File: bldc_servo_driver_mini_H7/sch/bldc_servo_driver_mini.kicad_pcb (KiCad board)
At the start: 4 copper layers, 35 x 40 mm, 68 parts, among them IC1 ST730MR, IC2 LDK320AM50R, IC3 TLT9251VLEXUMA1, J1 1-2328702-0, J2 Conn_01x04, J3 Conn_01x04, J4 Conn_01x06, J5 Conn_01x03, J6 Conn_01x02, J7 DF65-3P-1.7V_21_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

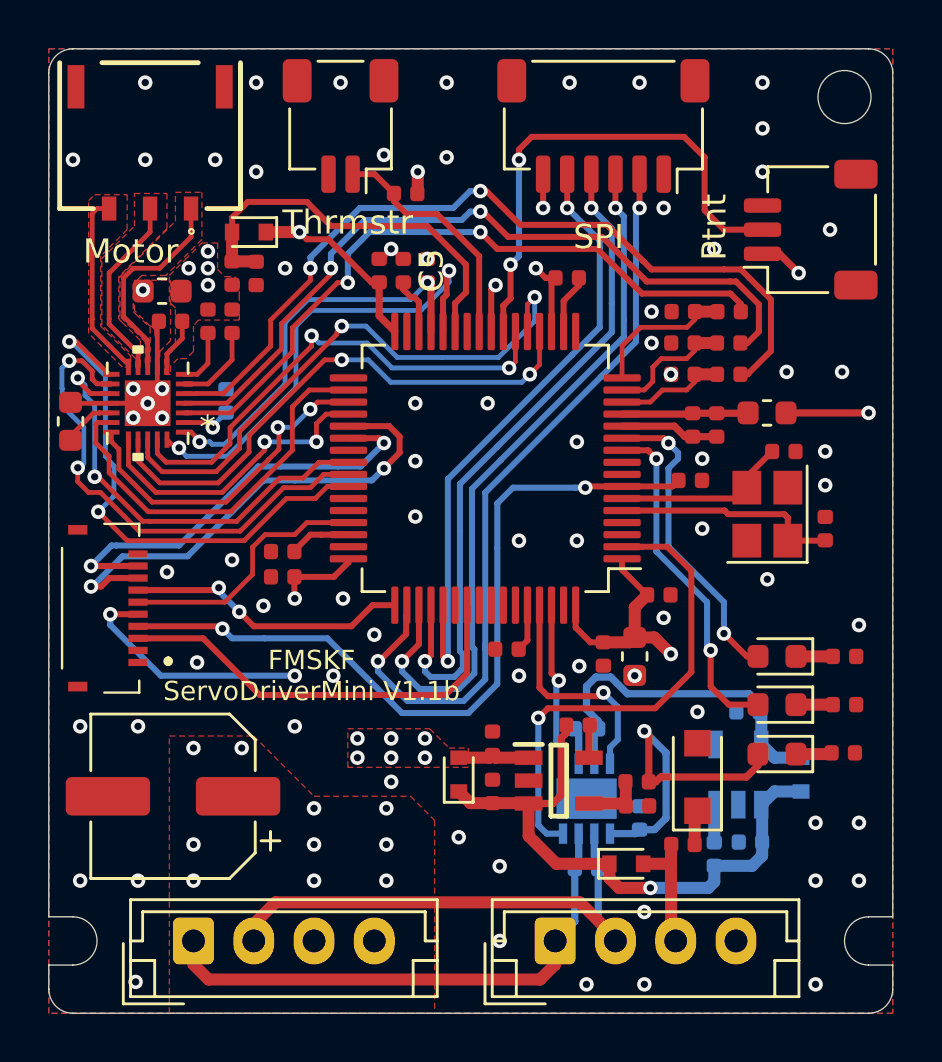
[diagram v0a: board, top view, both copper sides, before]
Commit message: fix : [H7sch] apply F4sch update to H7sch
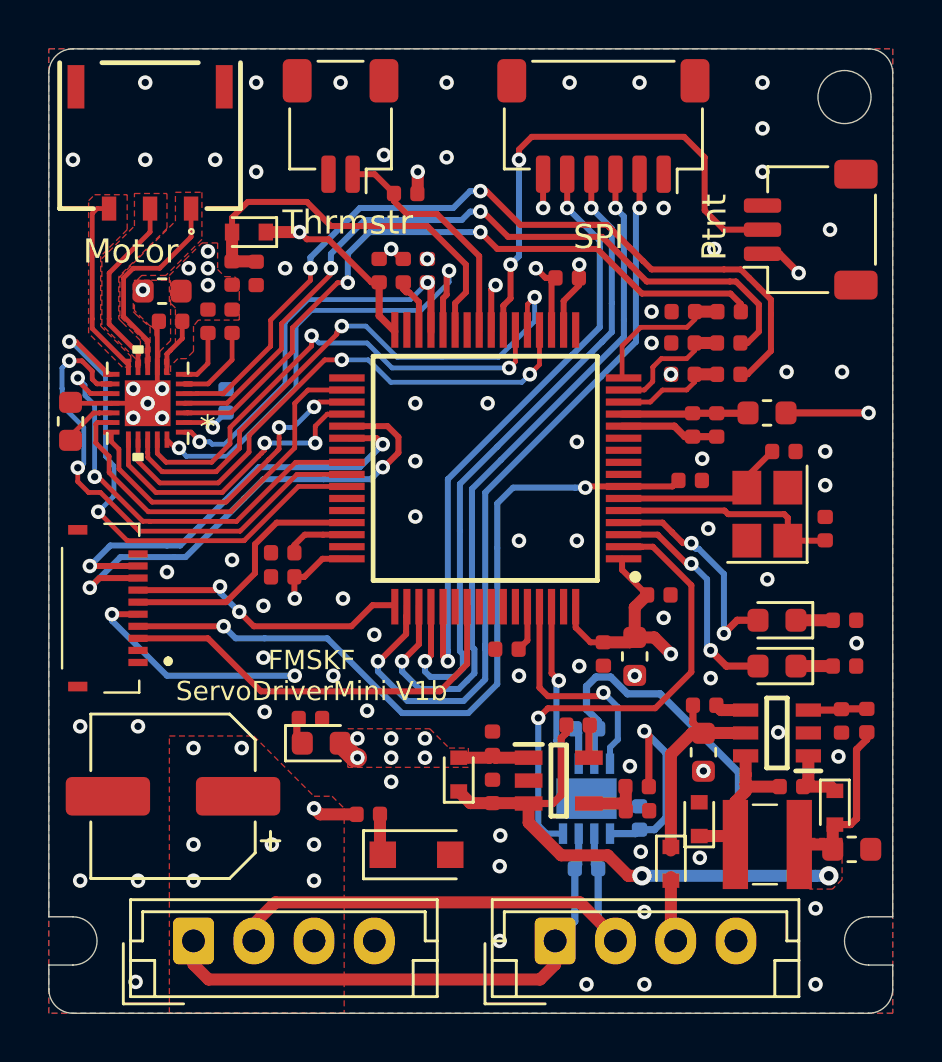
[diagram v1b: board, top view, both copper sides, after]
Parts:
- added C29: 10u, Capacitor_SMD:C_0603_1608Metric, F.Cu at (133.3, 93.2)
- added D9: D_Schottky, Diode_SMD:D_SOD-523, F.Cu at (132.6, 91.5)
- added L2: 4.7u, SamacSys_Parts:LPS3314332MRC, F.Cu at (129.8, 93.0)
- added R19: 30.1k, Resistor_SMD:R_0402_1005Metric, F.Cu at (133.9, 87.9)
- added R20: 10k, Resistor_SMD:R_0402_1005Metric, F.Cu at (132.9, 87.9)
- C15: value 1u -> 10u; footprint Capacitor_SMD:C_0402_1005Metric -> Capacitor_SMD:C_0603_1608Metric; moved to F.Cu
- C6: value 0.1u -> 0.01u; moved to F.Cu
- D2: value D_Schottky -> PMEG6010AESBYL
- D4, R3: moved to F.Cu
- IC2: value LDK320AM50R -> LT1616ES6#TRMPBF; footprint SamacSys_Parts:SOT95P280X145-5N -> SamacSys_Parts:SOT95P280X90-6N; moved to F.Cu
- U1: footprint Package_QFP:LQFP-64_10x10mm_P0.5mm -> SamacSys_Parts:QFP50P1200X1200X160-64N
- moved R14 22.1 mm to (110.8, 87.8)
- moved D8 18.9 mm to (111.3, 88.8), turned to 0 degrees
- moved R1 13.1 mm to (113.2, 91.8)
- moved C5 12.7 mm to (109.7, 80.9), turned to 180 degrees
- moved C2 12.7 mm to (114.7, 69.2), turned to 270 degrees
- moved D1 12.1 mm to (115.2, 93.4), turned to 0 degrees
- moved R3 6.19 mm to (127.2, 87.2), turned to 180 degrees
- moved D4 4.61 mm to (127.0, 92.0)
- moved C6 2.86 mm to (130.8, 90.6)
- moved C15 2.50 mm to (127.2, 89.2), turned to 90 degrees
- moved IC2 2.35 mm to (130.2, 88.4), turned to 180 degrees
- moved D2 1.85 mm to (125.8, 93.8), turned to 270 degrees
- moved D6 1.60 mm to (130.2, 85.6)
- moved R12 1.60 mm to (133.0, 85.6)
- moved D7 1.50 mm to (130.2, 83.7)
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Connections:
- C15 pad 1: +5V -> GND
- C15 pad 2: GND -> Net-(C15-Pad2)
- C5 pad 1: GND -> Net-(C5-Pad1)
- C5 pad 2: Net-(C5-Pad2) -> GND
- C6 pad 2: GND -> Net-(C6-Pad2)
- C8 pad 1: Net-(C6-Pad1) -> +5V
- D2 pad 1: Net-(C6-Pad1) -> Net-(C15-Pad2)
- D3 pad 1: Net-(C6-Pad1) -> +5V
- D4 pad 1: Net-(C6-Pad1) -> Net-(C6-Pad2)
- D4 pad 2: +5V -> GND
- IC1 pad 3: Net-(C6-Pad1) -> +5V
- IC2 pad 5: +5V -> Net-(C15-Pad2)
- R3 pad 1: Net-(C6-Pad1) -> Net-(IC2-Pad4)
- R3 pad 2: Net-(IC2-Pad3) -> Net-(C15-Pad2)
- R4 pad 1: Net-(C6-Pad1) -> +5V
- U1 pad 10: /LED1 -> Net-(U1-Pad10)
- U1 pad 11: /LED2 -> Net-(U1-Pad11)
- U1 pad 3: Net-(U1-Pad3) -> /LED1
- U1 pad 30: Net-(C5-Pad2) -> Net-(C2-Pad2)
- U1 pad 4: Net-(U1-Pad4) -> /LED2
- U1 pad 46: Net-(C2-Pad2) -> Net-(C5-Pad1)
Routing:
- net +5V: track 14.9 -> 46.0 mm, vias 0 -> 2
- net Net-(C6-Pad1): track 24.8 -> 2.75 mm, vias 1 -> 0
- net Net-(C15-Pad2): track 0.00 -> 8.80 mm
- net Net-(C6-Pad2): track 0.00 -> 6.95 mm
- net /LED1: track 14.2 -> 9.47 mm
- net /LED2: track 13.0 -> 9.18 mm
- net +3V3: track 155.5 -> 151.8 mm
- net Net-(C5-Pad1): track 0.00 -> 2.68 mm
- net Net-(C5-Pad2): track 2.39 -> 0.00 mm
- net Net-(IC2-Pad4): track 0.00 -> 1.30 mm
- net Net-(IC2-Pad3): track 1.59 -> 2.45 mm
- net +12V: track 8.23 -> 7.87 mm, vias 14 -> 12
- net GND: vias 74 -> 79
- added copper zone on F.Cu, net +5V
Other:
- board text added: "FMSKF ServoDriverMini V1b"
- board text removed: "FMSKF ServoDriverMini V1.1b"
